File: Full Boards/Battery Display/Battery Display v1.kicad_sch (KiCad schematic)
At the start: 193 parts, among them J2 Program Header, Q1 AO3401A, Q2 2N3904, Q3 AO3401A, Q4 2N3904, Q5 AO3401A, Q6 2N3904, SW1 SW_MEC_5G, SW2 SW_MEC_5G, U1 ISO1044BD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

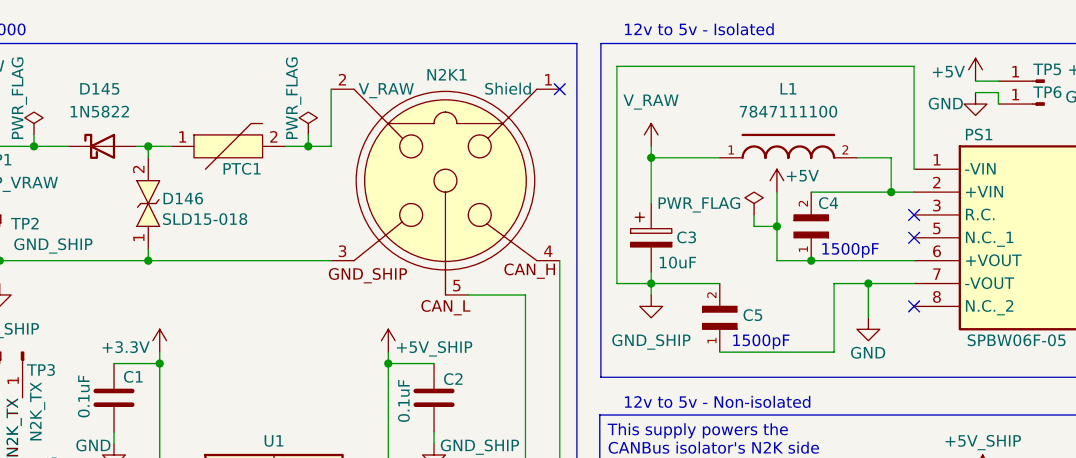
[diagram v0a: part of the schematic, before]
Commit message: Updated PCBs to swap RVS diodes from SLD15-018 to SLD22-018. Also swapped out the inductor from 7847111100 to PA4340.103NLT.
Signed-off-by: Madison Kelly <digital.mermaid@gmail.com>
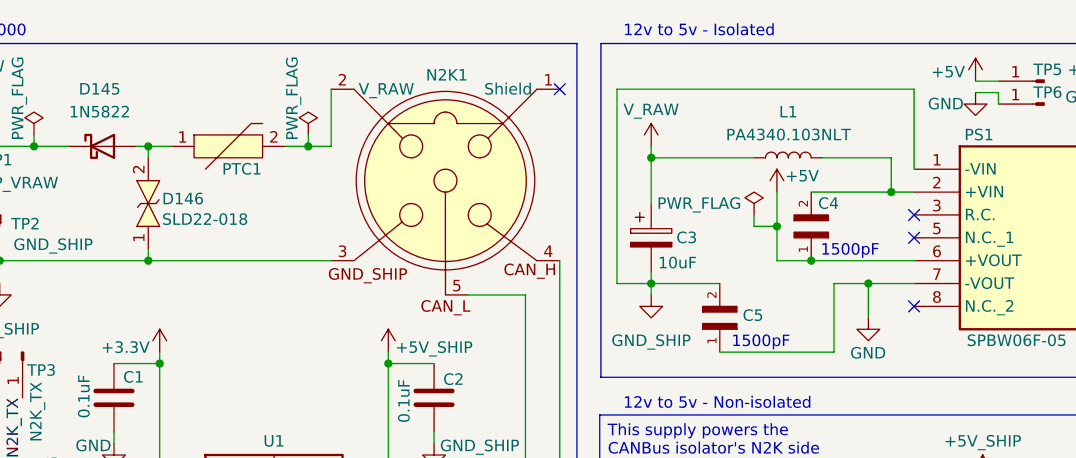
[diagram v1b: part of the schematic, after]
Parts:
- removed L1: 7847111100, mr-stuff:WE-RCIT_7847111100, symbol mr-parts:WE-RCIT
- added L1: PA4340.103NLT, mr-stuff:Pulse PA4340.103NLT, symbol Device:L
- D146: value SLD15-018 -> SLD22-018
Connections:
- net V_RAW: now also L1.1
- net at C4.2, PS1.2 (+VIN): now also L1.2
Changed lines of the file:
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@@
 	(wire
 		(pts
-			(xy 123.19 19.05) (xy 90.17 19.05)
+			(xy 123.19 21.59) (xy 90.17 21.59)
 		)
 		(stroke
@@
 	(wire
 		(pts
-			(xy 120.65 29.21) (xy 116.84 29.21)
-		)
-		(stroke
-			(width 0)
-			(type default)
-		)
-	)
-	(wire
-		(pts
 			(xy 158.75 21.59) (xy 166.37 21.59)
 		)
@@
 	(wire
 		(pts
+			(xy 113.03 29.21) (xy 120.65 29.21)
+		)
+		(stroke
+			(width 0)
+			(type default)
+		)
+	)
+	(wire
+		(pts
 			(xy 299.72 48.26) (xy 308.61 48.26)
 		)
@@
 	(wire
 		(pts
-			(xy 90.17 19.05) (xy 90.17 43.18)
+			(xy 90.17 21.59) (xy 90.17 43.18)
 		)
 		(stroke
@@
 	(wire
 		(pts
-			(xy 123.19 30.48) (xy 123.19 19.05)
+			(xy 123.19 30.48) (xy 123.19 21.59)
 		)
 		(stroke
@@
 	(wire
 		(pts
-			(xy 93.98 29.21) (xy 101.6 29.21)
+			(xy 93.98 29.21) (xy 105.41 29.21)
 		)
 		(stroke
@@
 	)
 	(symbol
+		(lib_id "Device:L")
+		(at 109.22 29.21 90)
+		(unit 1)
+		(exclude_from_sim no)
+		(in_bom yes)
+		(on_board yes)
+		(dnp no)
+		(fields_autoplaced yes)
+		(property "Reference" "L1"
+			(at 109.22 24.13 90)
+			(effects
+				(font
+					(size 1.27 1.27)
+				)
+			)
+		)
+		(property "Value" "PA4340.103NLT"
+			(at 109.22 26.67 90)
+			(effects
+				(font
+					(size 1.27 1.27)
+				)
+			)
+		)
+		(property "Footprint" "mr-stuff:Pulse PA4340.103NLT"
+			(at 109.22 29.21 0)
+			(effects
+				(font
+					(size 1.27 1.27)
+				)
+				(hide yes)
+			)
+		)
+		(property "Datasheet" "~"
+			(at 109.22 29.21 0)
+			(effects
+				(font
+					(size 1.27 1.27)
+				)
+				(hide yes)
+			)
+		)
+		(property "Description" "Inductor"
+			(at 109.22 29.21 0)
+			(effects
+				(font
+					(size 1.27 1.27)
+				)
+				(hide yes)
+			)
+		)
+		(pin "2"
+		)
+		(pin "1"
+		)
+		(instances
+			(project "Battery Display v1"
+				(path "/66b9b57f-ad5a-4774-9c04-72011a45113c"
+					(reference "L1")
+					(unit 1)
+				)
+			)
+		)
+	)
+	(symbol
 		(lib_id "power:GND")
 		(at 34.29 60.96 0)
@@
 		(on_board yes)
 		(dnp no)
-		(fields_autoplaced yes)
 		(property "Reference" "#PWR0134"
 			(at 93.98 31.75 0)
@@
 		)
 		(property "Value" "V_RAW"
-			(at 93.98 22.86 0)
+			(at 93.98 23.876 0)
 			(effects
 				(font
@@
 	)
 	(symbol
-		(lib_id "mr-parts:WE-RCIT")
-		(at 109.22 29.21 0)
-		(unit 1)
-		(exclude_from_sim no)
-		(in_bom yes)
-		(on_board yes)
-		(dnp no)
-		(fields_autoplaced yes)
-		(property "Reference" "L1"
-			(at 109.22 21.59 0)
-			(effects
-				(font
-					(size 1.27 1.27)
-				)
-			)
-		)
-		(property "Value" "7847111100"
-			(at 109.22 24.13 0)
-			(effects
-				(font
-					(size 1.27 1.27)
-				)
-			)
-		)
-		(property "Footprint" "mr-stuff:WE-RCIT_7847111100"
-			(at 109.474 34.29 0)
-			(effects
-				(font
-					(size 1.27 1.27)
-				)
-				(justify bottom)
-				(hide yes)
-			)
-		)
-		(property "Datasheet" "https://www.we-online.com/components/products/datasheet/7847111100.pdf"
-			(at 109.22 29.21 0)
-			(effects
-				(font
-					(size 1.27 1.27)
-				)
-				(hide yes)
-			)
-		)
-		(property "Description" "10uH, 3A, rod-core inductor"
-			(at 109.22 29.21 0)
-			(effects
-				(font
-					(size 1.27 1.27)
-				)
-				(hide yes)
-			)
-		)
-		(pin "2"
-		)
-		(pin "1"
-		)
-		(instances
-			(project "Battery Display v1"
-				(path "/66b9b57f-ad5a-4774-9c04-72011a45113c"
-					(reference "L1")
-					(unit 1)
-				)
-			)
-		)
-	)
-	(symbol
 		(lib_id "Device:LED")
 		(at 287.02 21.59 180)
@@
 			)
 		)
-		(property "Value" "SLD15-018"
+		(property "Value" "SLD22-018"
 			(at 39.624 36.068 90)
 			(effects

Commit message: Updated boards and schematics.
These are the version that have been ordered. Any further changes will be a new version.

Signed-off-by: Madison Kelly <digital.mermaid@gmail.com>
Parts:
- removed C5: TDK FA28NP01H152JNU06, FA28NP01H152JNU06:CAPRB500W50L400T250H550, symbol mr-parts:TDK FA28NP01H152JNU06
- removed D100, D101, D102, D103, D104, D105, D106, D107: 1N5822, Diode_THT:D_DO-41_SOD81_P10.16mm_Horizontal, symbol Diode:1N4001
- added C25, C26, C27, C28, C5: 0.1uF, mr-stuff:RCE5C1H104J2A2H03B, symbol Device:C
- added J1: Future Bonding, Connector_PinHeader_2.54mm:PinHeader_1x03_P2.54mm_Horizontal, symbol Connector:Conn_01x03_Pin
- added R24, R25, R26, R27: 3.3K, Resistor_THT:R_Axial_DIN0207_L6.3mm_D2.5mm_P7.62mm_Horizontal, symbol Device:R
- C4: footprint FA28NP01H152JNU06:CAPRB500W50L400T250H550 -> mr-stuff:TDK CAPRB500W50L400T250H550
- D146: footprint DIOAD4425W136L885D885 -> mr-stuff:DIOAD4425W136L885D885
- PS1: footprint SPBW06F05 -> mr-stuff:SPBW06F05
- R1: now fitted
- R21, R22, R23, R89: value 10 -> 475
- U5: symbol Interface_UART:MAX3232 -> mr-parts:TI MAX3232EIPWRQ1
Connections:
- net +3.3V: now also U5.10 (T2IN), R24.1, R25.1, R26.1, R27.1
- net BOARD_I2C_SCL: now also R27.2
- net BOARD_I2C_SDA: now also R26.2
- net BRIGHTNESS_POT_IN: now also C25.1
- net DISPLAY_ON_IN: now also C28.1
- net GND: now also C25.2, C26.2, C27.2, C28.2, C5.2, J1.2 (Pin_2)
- net GND_SHIP: now also C5.1, J1.3 (Pin_3)
- net IS31_I2C_SCL: now also R25.2
- net IS31_I2C_SDA: now also R24.2
- net LCD_PGDOWN_IN: now also C27.1
- net LCD_PGUP_IN: now also C26.1
- net at N2K1.1: now also J1.1 (Pin_1)
- no-connect marks 28 -> 26
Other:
- moved on the sheet: C12, C19, C20, C21, C22, C23, C24, C3, C4, C6, C7, C8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
